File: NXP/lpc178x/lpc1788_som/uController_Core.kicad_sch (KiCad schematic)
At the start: 1 part, among them U201 LPC1788FBD208

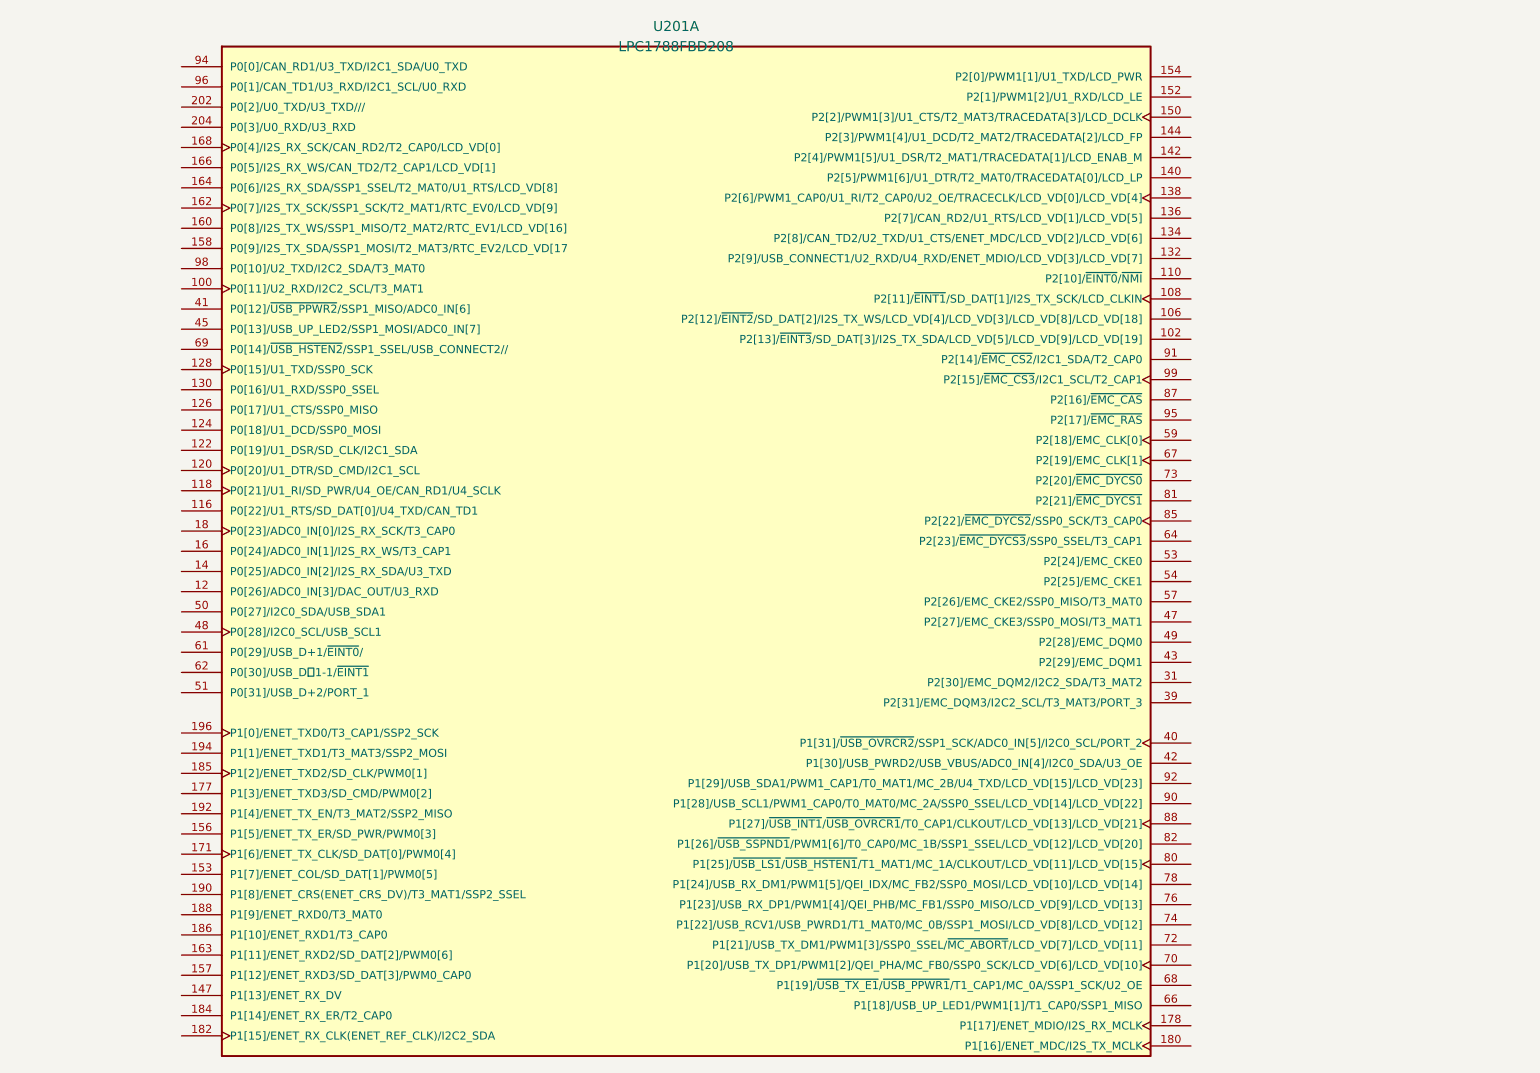
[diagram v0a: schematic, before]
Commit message: Add sodim connector
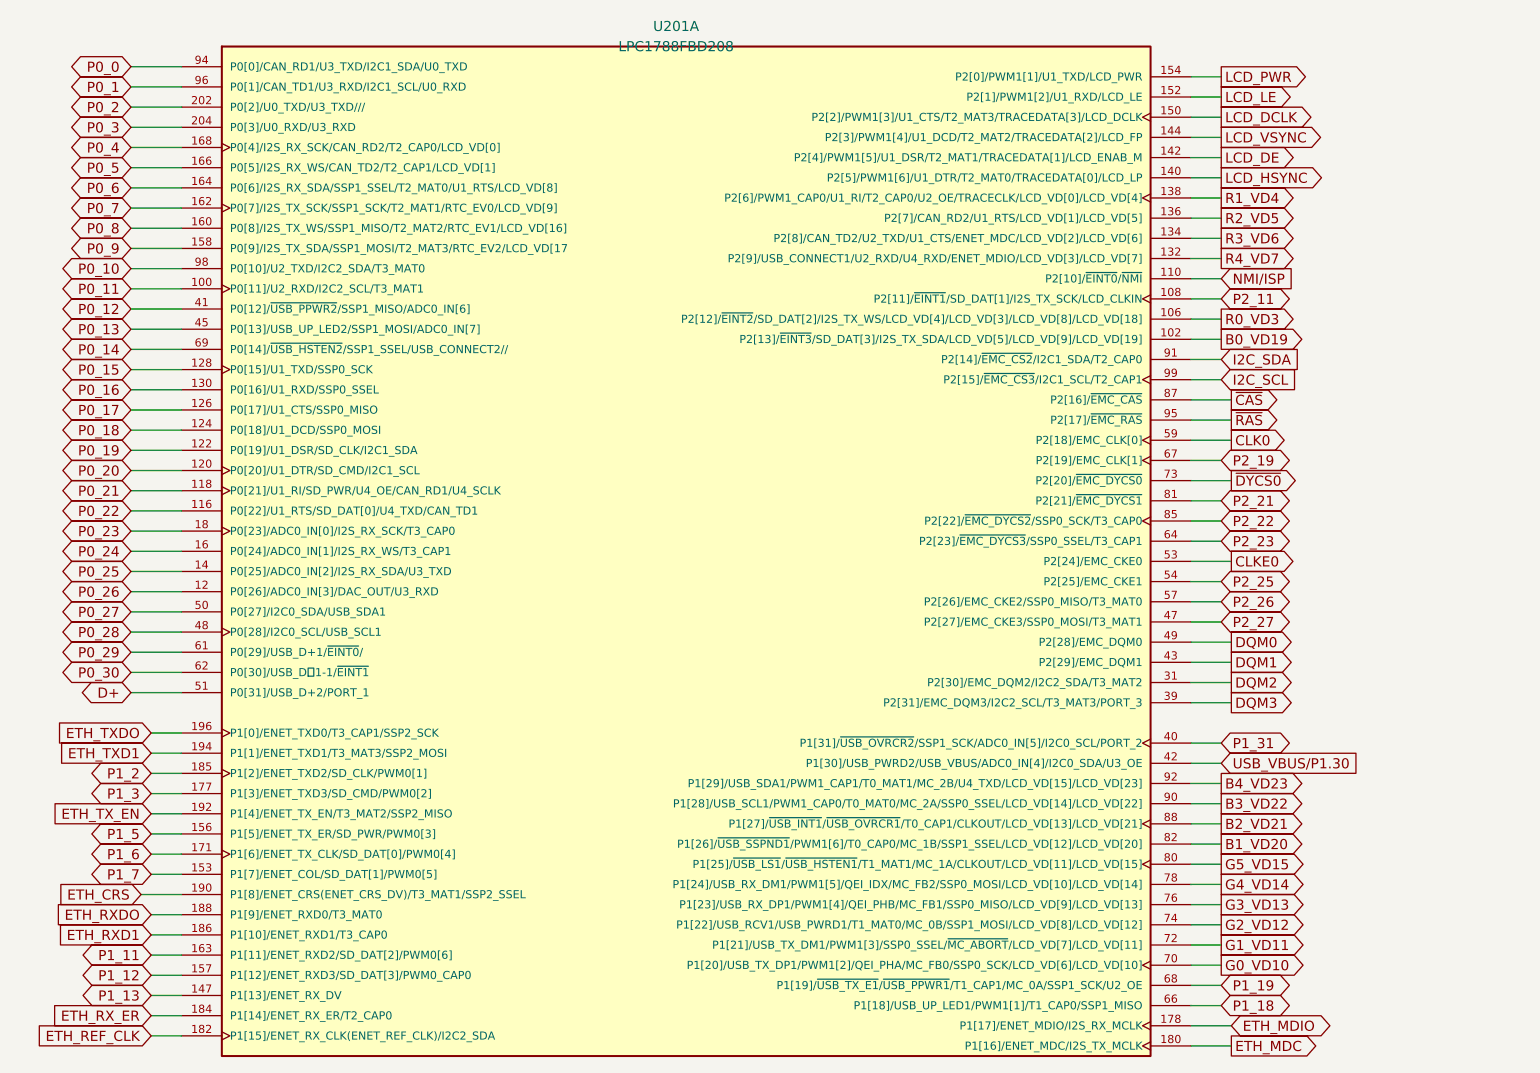
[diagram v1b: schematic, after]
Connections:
- net P0_11: now reaches U201.100 (P0[11]/U2_RXD/I2C2_SCL/T3_MAT1)
- net B0_VD19: now reaches U201.102 (P2[13]/~{EINT3}/SD_DAT[3]/I2S_TX_SDA/LCD_VD[5]/LCD_VD[9]/LCD_VD[19])
- net R0_VD3: now reaches U201.106 (P2[12]/~{EINT2}/SD_DAT[2]/I2S_TX_WS/LCD_VD[4]/LCD_VD[3]/LCD_VD[8]/LCD_VD[18])
- net P2_11: now reaches U201.108 (P2[11]/~{EINT1}/SD_DAT[1]/I2S_TX_SCK/LCD_CLKIN)
- net NMI/ISP: now reaches U201.110 (P2[10]/~{EINT0}/~{NMI})
- net P0_22: now reaches U201.116 (P0[22]/U1_RTS/SD_DAT[0]/U4_TXD/CAN_TD1)
- net P0_21: now reaches U201.118 (P0[21]/U1_RI/SD_PWR/U4_OE/CAN_RD1/U4_SCLK)
- net P0_26: now reaches U201.12 (P0[26]/ADC0_IN[3]/DAC_OUT/U3_RXD)
- net P0_20: now reaches U201.120 (P0[20]/U1_DTR/SD_CMD/I2C1_SCL)
- net P0_19: now reaches U201.122 (P0[19]/U1_DSR/SD_CLK/I2C1_SDA)
- net P0_18: now reaches U201.124 (P0[18]/U1_DCD/SSP0_MOSI)
- net P0_17: now reaches U201.126 (P0[17]/U1_CTS/SSP0_MISO)
- net P0_15: now reaches U201.128 (P0[15]/U1_TXD/SSP0_SCK)
- net P0_16: now reaches U201.130 (P0[16]/U1_RXD/SSP0_SSEL)
- net R4_VD7: now reaches U201.132 (P2[9]/USB_CONNECT1/U2_RXD/U4_RXD/ENET_MDIO/LCD_VD[3]/LCD_VD[7])
- net R3_VD6: now reaches U201.134 (P2[8]/CAN_TD2/U2_TXD/U1_CTS/ENET_MDC/LCD_VD[2]/LCD_VD[6])
- net R2_VD5: now reaches U201.136 (P2[7]/CAN_RD2/U1_RTS/LCD_VD[1]/LCD_VD[5])
- net R1_VD4: now reaches U201.138 (P2[6]/PWM1_CAP0/U1_RI/T2_CAP0/U2_OE/TRACECLK/LCD_VD[0]/LCD_VD[4])
- net P0_25: now reaches U201.14 (P0[25]/ADC0_IN[2]/I2S_RX_SDA/U3_TXD)
- net LCD_HSYNC: now reaches U201.140 (P2[5]/PWM1[6]/U1_DTR/T2_MAT0/TRACEDATA[0]/LCD_LP)
- net LCD_DE: now reaches U201.142 (P2[4]/PWM1[5]/U1_DSR/T2_MAT1/TRACEDATA[1]/LCD_ENAB_M)
- net LCD_VSYNC: now reaches U201.144 (P2[3]/PWM1[4]/U1_DCD/T2_MAT2/TRACEDATA[2]/LCD_FP)
- net P1_13: now reaches U201.147 (P1[13]/ENET_RX_DV)
- net LCD_DCLK: now reaches U201.150 (P2[2]/PWM1[3]/U1_CTS/T2_MAT3/TRACEDATA[3]/LCD_DCLK)
- net LCD_LE: now reaches U201.152 (P2[1]/PWM1[2]/U1_RXD/LCD_LE)
- net P1_7: now reaches U201.153 (P1[7]/ENET_COL/SD_DAT[1]/PWM0[5])
- net LCD_PWR: now reaches U201.154 (P2[0]/PWM1[1]/U1_TXD/LCD_PWR)
- net P1_5: now reaches U201.156 (P1[5]/ENET_TX_ER/SD_PWR/PWM0[3])
- net P1_12: now reaches U201.157 (P1[12]/ENET_RXD3/SD_DAT[3]/PWM0_CAP0)
- net P0_9: now reaches U201.158 (P0[9]/I2S_TX_SDA/SSP1_MOSI/T2_MAT3/RTC_EV2/LCD_VD[17)
- net P0_24: now reaches U201.16 (P0[24]/ADC0_IN[1]/I2S_RX_WS/T3_CAP1)
- net P0_8: now reaches U201.160 (P0[8]/I2S_TX_WS/SSP1_MISO/T2_MAT2/RTC_EV1/LCD_VD[16])
- net P0_7: now reaches U201.162 (P0[7]/I2S_TX_SCK/SSP1_SCK/T2_MAT1/RTC_EV0/LCD_VD[9])
- net P1_11: now reaches U201.163 (P1[11]/ENET_RXD2/SD_DAT[2]/PWM0[6])
- net P0_6: now reaches U201.164 (P0[6]/I2S_RX_SDA/SSP1_SSEL/T2_MAT0/U1_RTS/LCD_VD[8])
- net P0_5: now reaches U201.166 (P0[5]/I2S_RX_WS/CAN_TD2/T2_CAP1/LCD_VD[1])
- net P0_4: now reaches U201.168 (P0[4]/I2S_RX_SCK/CAN_RD2/T2_CAP0/LCD_VD[0])
- net P1_6: now reaches U201.171 (P1[6]/ENET_TX_CLK/SD_DAT[0]/PWM0[4])
- net P1_3: now reaches U201.177 (P1[3]/ENET_TXD3/SD_CMD/PWM0[2])
- net ETH_MDIO: now reaches U201.178 (P1[17]/ENET_MDIO/I2S_RX_MCLK)
- net P0_23: now reaches U201.18 (P0[23]/ADC0_IN[0]/I2S_RX_SCK/T3_CAP0)
- net ETH_MDC: now reaches U201.180 (P1[16]/ENET_MDC/I2S_TX_MCLK)
- net ETH_REF_CLK: now reaches U201.182 (P1[15]/ENET_RX_CLK(ENET_REF_CLK)/I2C2_SDA)
- net ETH_RX_ER: now reaches U201.184 (P1[14]/ENET_RX_ER/T2_CAP0)
- net P1_2: now reaches U201.185 (P1[2]/ENET_TXD2/SD_CLK/PWM0[1])
- net ETH_RXD1: now reaches U201.186 (P1[10]/ENET_RXD1/T3_CAP0)
- net ETH_RXDO: now reaches U201.188 (P1[9]/ENET_RXD0/T3_MAT0)
- net ETH_CRS: now reaches U201.190 (P1[8]/ENET_CRS(ENET_CRS_DV)/T3_MAT1/SSP2_SSEL)
- net ETH_TX_EN: now reaches U201.192 (P1[4]/ENET_TX_EN/T3_MAT2/SSP2_MISO)
- net ETH_TXD1: now reaches U201.194 (P1[1]/ENET_TXD1/T3_MAT3/SSP2_MOSI)
- net ETH_TXDO: now reaches U201.196 (P1[0]/ENET_TXD0/T3_CAP1/SSP2_SCK)
- net P0_2: now reaches U201.202 (P0[2]/U0_TXD/U3_TXD///)
- net P0_3: now reaches U201.204 (P0[3]/U0_RXD/U3_RXD)
- net DQM2: now reaches U201.31 (P2[30]/EMC_DQM2/I2C2_SDA/T3_MAT2)
- net DQM3: now reaches U201.39 (P2[31]/EMC_DQM3/I2C2_SCL/T3_MAT3/PORT_3)
- net P1_31: now reaches U201.40 (P1[31]/~{USB_OVRCR2}/SSP1_SCK/ADC0_IN[5]/I2C0_SCL/PORT_2)
- net P0_12: now reaches U201.41 (P0[12]/~{USB_PPWR2}/SSP1_MISO/ADC0_IN[6])
- net USB_VBUS/P1.30: now reaches U201.42 (P1[30]/USB_PWRD2/USB_VBUS/ADC0_IN[4]/I2C0_SDA/U3_OE)
- net DQM1: now reaches U201.43 (P2[29]/EMC_DQM1)
- net P0_13: now reaches U201.45 (P0[13]/USB_UP_LED2/SSP1_MOSI/ADC0_IN[7])
- net P2_27: now reaches U201.47 (P2[27]/EMC_CKE3/SSP0_MOSI/T3_MAT1)
- net P0_28: now reaches U201.48 (P0[28]/I2C0_SCL/USB_SCL1)
- net DQM0: now reaches U201.49 (P2[28]/EMC_DQM0)
- net P0_27: now reaches U201.50 (P0[27]/I2C0_SDA/USB_SDA1)
- net D+: now reaches U201.51 (P0[31]/USB_D+2/PORT_1)
- net CLKE0: now reaches U201.53 (P2[24]/EMC_CKE0)
- net P2_25: now reaches U201.54 (P2[25]/EMC_CKE1)
- net P2_26: now reaches U201.57 (P2[26]/EMC_CKE2/SSP0_MISO/T3_MAT0)
- net CLK0: now reaches U201.59 (P2[18]/EMC_CLK[0])
- net P0_29: now reaches U201.61 (P0[29]/USB_D+1/~{EINT0}/)
- net P0_30: now reaches U201.62 (P0[30]/USB_D1-1/~{EINT1})
- net P2_23: now reaches U201.64 (P2[23]/~{EMC_DYCS3}/SSP0_SSEL/T3_CAP1)
- net P1_18: now reaches U201.66 (P1[18]/USB_UP_LED1/PWM1[1]/T1_CAP0/SSP1_MISO)
- net P2_19: now reaches U201.67 (P2[19]/EMC_CLK[1])
- net P1_19: now reaches U201.68 (P1[19]/~{USB_TX_E1}/~{USB_PPWR1}/T1_CAP1/MC_0A/SSP1_SCK/U2_OE)
- net P0_14: now reaches U201.69 (P0[14]/~{USB_HSTEN2}/SSP1_SSEL/USB_CONNECT2//)
- net G0_VD10: now reaches U201.70 (P1[20]/USB_TX_DP1/PWM1[2]/QEI_PHA/MC_FB0/SSP0_SCK/LCD_VD[6]/LCD_VD[10])
- net G1_VD11: now reaches U201.72 (P1[21]/USB_TX_DM1/PWM1[3]/SSP0_SSEL/~{MC_ABORT}/LCD_VD[7]/LCD_VD[11])
- net ~{DYCS0}: now reaches U201.73 (P2[20]/~{EMC_DYCS0})
- net G2_VD12: now reaches U201.74 (P1[22]/USB_RCV1/USB_PWRD1/T1_MAT0/MC_0B/SSP1_MOSI/LCD_VD[8]/LCD_VD[12])
- net G3_VD13: now reaches U201.76 (P1[23]/USB_RX_DP1/PWM1[4]/QEI_PHB/MC_FB1/SSP0_MISO/LCD_VD[9]/LCD_VD[13])
- net G4_VD14: now reaches U201.78 (P1[24]/USB_RX_DM1/PWM1[5]/QEI_IDX/MC_FB2/SSP0_MOSI/LCD_VD[10]/LCD_VD[14])
- net G5_VD15: now reaches U201.80 (P1[25]/~{USB_LS1}/~{USB_HSTEN1}/T1_MAT1/MC_1A/CLKOUT/LCD_VD[11]/LCD_VD[15])
- net P2_21: now reaches U201.81 (P2[21]/~{EMC_DYCS1})
- net B1_VD20: now reaches U201.82 (P1[26]/~{USB_SSPND1}/PWM1[6]/T0_CAP0/MC_1B/SSP1_SSEL/LCD_VD[12]/LCD_VD[20])
- net P2_22: now reaches U201.85 (P2[22]/~{EMC_DYCS2}/SSP0_SCK/T3_CAP0)
- net ~{CAS}: now reaches U201.87 (P2[16]/~{EMC_CAS})
- net B2_VD21: now reaches U201.88 (P1[27]/~{USB_INT1}/~{USB_OVRCR1}/T0_CAP1/CLKOUT/LCD_VD[13]/LCD_VD[21])
- net B3_VD22: now reaches U201.90 (P1[28]/USB_SCL1/PWM1_CAP0/T0_MAT0/MC_2A/SSP0_SSEL/LCD_VD[14]/LCD_VD[22])
- net I2C_SDA: now reaches U201.91 (P2[14]/~{EMC_CS2}/I2C1_SDA/T2_CAP0)
- net B4_VD23: now reaches U201.92 (P1[29]/USB_SDA1/PWM1_CAP1/T0_MAT1/MC_2B/U4_TXD/LCD_VD[15]/LCD_VD[23])
- net P0_0: now reaches U201.94 (P0[0]/CAN_RD1/U3_TXD/I2C1_SDA/U0_TXD)
- net ~{RAS}: now reaches U201.95 (P2[17]/~{EMC_RAS})
- net P0_1: now reaches U201.96 (P0[1]/CAN_TD1/U3_RXD/I2C1_SCL/U0_RXD)
- net P0_10: now reaches U201.98 (P0[10]/U2_TXD/I2C2_SDA/T3_MAT0)
- net I2C_SCL: now reaches U201.99 (P2[15]/~{EMC_CS3}/I2C1_SCL/T2_CAP1)

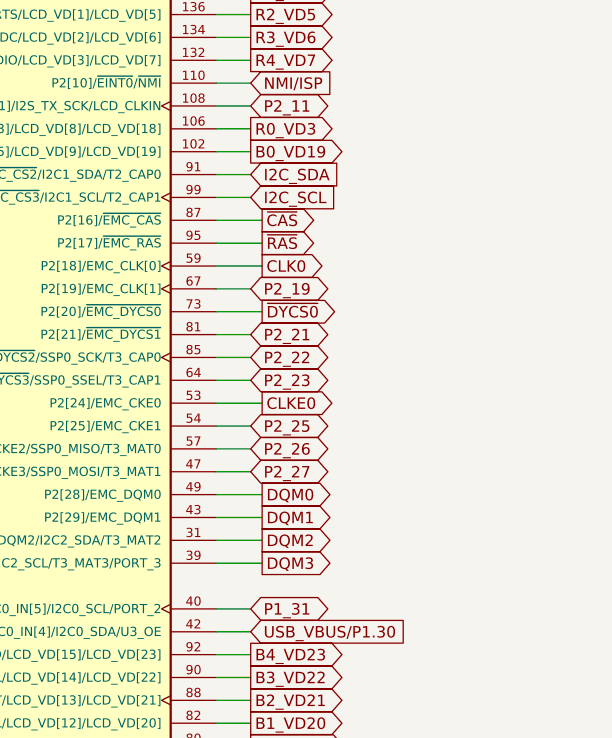
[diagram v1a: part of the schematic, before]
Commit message: LPC1788
Added LPC1788 som module
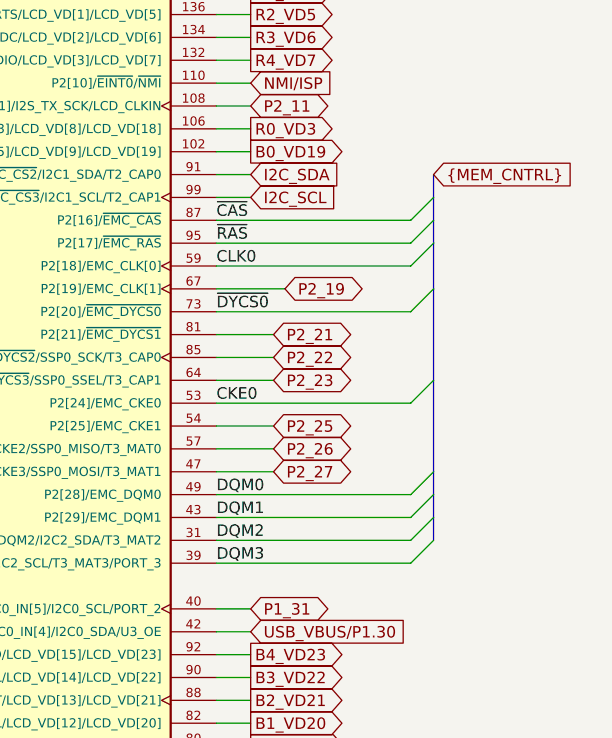
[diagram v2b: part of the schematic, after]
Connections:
- net CLKE0 renamed CKE0
